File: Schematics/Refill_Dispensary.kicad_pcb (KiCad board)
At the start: 2 copper layers, 7.5 x 2 mm, 60 parts, among them J1 USB_B_Micro, J10 Switch 2, J11 Switch 3, J12 Switch 1, J2 Pot 1, J3 Barrel_Jack_Switch, J4 USB_BOOT, J5 Load Cell Power, J6 Load Cell Data, J7 Inductor 1, J8 Inductor 2, J9 Pot 2, Q1 TIP120, Q2 TIP120, SW4 SW_SPDT, U1 RP2040, U2 NCP1117-3.3_SOT223, U3 Flash Memory, U4 NHD-C0220BIZ, U5 AD622, Y1 Crystal

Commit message: organizing
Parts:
- moved J7 225.0 mm to (255.0, 144.9), turned to -90 degrees
- moved J8 207.7 mm to (255.8, 122.4), turned to -90 degrees
- moved R3 112.9 mm to (19.9, 59.1)
- moved R2 108.4 mm to (30.4, 58.5)
- moved J6 108.3 mm to (14.7, 164.6), turned to 90 degrees
- moved R1 105.1 mm to (40.6, 58.5), turned to 180 degrees
- moved J11 103.2 mm to (112.3, 68.6), turned to 180 degrees
- moved Q1 96.5 mm to (243.5, 136.1)
- moved J1 90.1 mm to (170.9, 33.8)
- moved J10 88.3 mm to (100.3, 68.8), turned to 180 degrees
- moved D3 86.9 mm to (17.4, 59.2), turned to 180 degrees
- moved C2 84.6 mm to (151.1, 50.2), turned to -90 degrees
- moved U2 84.1 mm to (158.6, 49.0), turned to -90 degrees
- moved C3 82.9 mm to (167.0, 51.4), turned to 90 degrees
- moved D2 81.0 mm to (27.6, 58.8), turned to 180 degrees
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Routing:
- net GND: vias 0 -> 2
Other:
- outline, holes or cut-outs redrawn
- board text added: "Load Cell"
- board text added: "Machine Status LEDs"
- board text added: "Notes: R1 is unconnected"
- board text added: "Power Supply"
- board text added: "UI Go Buttons"
- board text added: "User Interface"
- board text added: "Valve Control"

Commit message: everything is pretty
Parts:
- moved 1u1 142.0 mm to (55.6, 53.2), turned to 90 degrees
- moved C9 114.3 mm to (193.0, 79.9)
- moved C13 108.8 mm to (193.3, 84.8)
- moved C10 97.2 mm to (193.8, 95.1)
- moved C7 92.2 mm to (95.5, 87.9), turned to 180 degrees
- moved 10k2 91.9 mm to (104.8, 80.1), turned to 180 degrees
- moved C11 87.0 mm to (193.4, 89.6)
- moved C1 85.5 mm to (95.6, 92.3), turned to 180 degrees
- moved C12 83.6 mm to (102.7, 97.5)
- moved C6 73.6 mm to (79.3, 151.1), turned to 90 degrees
- moved R15 72.8 mm to (111.0, 101.2)
- moved R9 72.8 mm to (115.4, 101.2)
- moved R7 72.4 mm to (137.3, 153.3)
- moved C8 71.5 mm to (97.2, 97.7)
- moved C5 64.2 mm to (96.9, 151.1), turned to 90 degrees
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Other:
- outline, holes or cut-outs redrawn
- board text added: "Flash Mem"

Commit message: I'm cant make a PCB
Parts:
- added R13: 10k, Resistor_SMD:R_0201_0603Metric, F.Cu at (85.7, 65.3)
- R10: value R -> 10k
- moved J6 165.8 mm to (202.1, 105.4), turned to -90 degrees
- moved R12 135.6 mm to (178.4, 113.3), turned to 0 degrees
- moved U5 117.6 mm to (170.8, 106.0), turned to 90 degrees
- moved D6 117.0 mm to (164.5, 112.1), turned to 90 degrees
- moved D7 106.2 mm to (164.1, 101.4), turned to 90 degrees
- moved C13 100.3 mm to (95.5, 106.9)
- moved C11 95.1 mm to (102.2, 116.6), turned to 90 degrees
- moved J4 94.6 mm to (64.8, 85.1)
- moved R7 90.3 mm to (69.3, 93.9)
- moved C9 87.8 mm to (108.8, 105.0), turned to 180 degrees
- moved J5 84.5 mm to (107.6, 79.0), turned to 0 degrees
- moved C10 84.2 mm to (111.0, 110.5), turned to 180 degrees
- moved J11 71.4 mm to (48.6, 101.0), turned to -90 degrees
- moved R10 69.1 mm to (95.3, 67.4)
- moved J12 68.5 mm to (49.0, 125.6), turned to -90 degrees
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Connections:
- net Net-(C1-Pad2) renamed +1V1
- net Net-(C5-Pad2) renamed /CLK_IN
- net Net-(R11-Pad2) renamed /CLK_OUT
- D4 pad 1: Net-(J7-Pad1) -> GND
- D4 pad 2: +12V -> Net-(D4-Pad2)
- D5 pad 1: Net-(D5-Pad1) -> GND
- D5 pad 2: +12V -> Net-(D5-Pad2)
- J7 pad 1: Net-(J7-Pad1) -> GND
- J7 pad 2: +12V -> Net-(D4-Pad2)
- J8 pad 1: Net-(D5-Pad1) -> GND
- J8 pad 2: +12V -> Net-(D5-Pad2)
- Q1 pad 2: Net-(J7-Pad1) -> +12V
- Q1 pad 3: GND -> Net-(D4-Pad2)
- Q2 pad 2: Net-(D5-Pad1) -> +12V
- Q2 pad 3: GND -> Net-(D5-Pad2)
- R1 pad 1: unconnected-(R1-Pad1) -> GND
- U1 pad 4: unconnected-(U1-Pad4) -> /S_SDA
- U1 pad 5: unconnected-(U1-Pad5) -> /S_SCL
- U1 pad 6: /S_SDA -> unconnected-(U1-Pad6)
- U1 pad 7: /S_SCL -> unconnected-(U1-Pad7)
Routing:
- net +3.3V: track 0.00 -> 31.7 mm
- net Net-(C2-Pad1): track 0.00 -> 13.6 mm
- net +12V: track 0.00 -> 11.7 mm
- net Net-(J1-Pad1): track 0.00 -> 10.2 mm
- net +1V1: track 0.00 -> 9.89 mm
- net Net-(R15-Pad2): track 0.00 -> 5.68 mm
- net GND: track 0.00 -> 4.93 mm, vias 2 -> 1
- net Net-(R9-Pad2): track 0.00 -> 4.24 mm
- removed copper zone on B.Cu, net GND
- removed copper zone on F.Cu, net GND
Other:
- board text removed: "Flash Mem"
- board text removed: "Load Cell"
- board text removed: "Valve Control"

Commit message: I'm cant make a PCB again
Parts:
- removed 10k2: R, Resistor_SMD:R_0201_0603Metric
- removed 1u1: C, Capacitor_SMD:C_0201_0603Metric
- added ?: , , F.Cu at (102.4, 110.7)
- added ?: , , F.Cu at (101.0, 109.3)
- added ?: , , F.Cu at (103.6, 110.7)
- added ?: , , F.Cu at (101.0, 108.2)
- added ?: , , F.Cu at (102.4, 108.2)
- added ?: , , F.Cu at (101.0, 110.7)
- added ?: , , F.Cu at (103.6, 109.3)
- added ?: , , F.Cu at (103.6, 108.2)
- added ?: , , F.Cu at (102.4, 109.3)
- added C14: 1u, Capacitor_SMD:C_0201_0603Metric, F.Cu at (97.8, 168.3)
- moved J7 148.5 mm to (57.5, 97.2), turned to 90 degrees
- moved J8 143.6 mm to (57.3, 109.0), turned to 90 degrees
- moved H1 127.1 mm to (179.3, 56.5)
- moved H2 127.1 mm to (173.6, 50.8)
- moved H3 127.1 mm to (173.6, 56.5)
- moved H4 127.1 mm to (179.3, 50.8)
- moved U4 124.4 mm to (103.8, 149.2)
- moved D5 123.2 mm to (67.6, 95.8), turned to 90 degrees
- moved D4 122.6 mm to (72.7, 95.1), turned to 90 degrees
- moved Q1 105.6 mm to (73.7, 101.7), turned to 180 degrees
- moved Q2 100.3 mm to (73.4, 109.2), turned to 180 degrees
- moved D3 99.5 mm to (55.3, 152.2), turned to -90 degrees
- moved R3 96.8 mm to (59.7, 151.9), turned to 180 degrees
- moved D2 90.2 mm to (55.3, 145.8), turned to -90 degrees
- moved R2 87.0 mm to (59.7, 145.9), turned to 180 degrees
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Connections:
- D4 pad 1: GND -> Net-(D4-Pad1)
- D4 pad 2: Net-(D4-Pad2) -> +12V
- D5 pad 1: GND -> Net-(D5-Pad1)
- D5 pad 2: Net-(D5-Pad2) -> +12V
- J7 pad 1: GND -> Net-(D4-Pad1)
- J7 pad 2: Net-(D4-Pad2) -> +12V
- J8 pad 1: GND -> Net-(D5-Pad1)
- J8 pad 2: Net-(D5-Pad2) -> +12V
- Q1 pad 2: +12V -> Net-(D4-Pad1)
- Q1 pad 3: Net-(D4-Pad2) -> GND
- Q2 pad 2: +12V -> Net-(D5-Pad1)
- Q2 pad 3: Net-(D5-Pad2) -> GND
- U1 pad 11: /LED3 -> unconnected-(U1-Pad11)
- U1 pad 15: unconnected-(U1-Pad15) -> /LED1
- U1 pad 16: unconnected-(U1-Pad16) -> /LED2
- U1 pad 17: unconnected-(U1-Pad17) -> /LED3
- U1 pad 8: /LED1 -> unconnected-(U1-Pad8)
- U1 pad 9: /LED2 -> unconnected-(U1-Pad9)
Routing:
- net +12V: track 11.7 -> 95.5 mm
- net /S_SCL: track 0.00 -> 67.1 mm, vias 0 -> 1
- net /S_SDA: track 0.00 -> 66.8 mm, vias 0 -> 1
- net /LED3: track 0.00 -> 64.2 mm
- net /LED2: track 0.00 -> 60.8 mm
- net /USB_D+: track 0.00 -> 60.3 mm, vias 0 -> 2
- net /LED1: track 0.00 -> 56.4 mm
- net /SW3: track 0.00 -> 53.8 mm
- net /SW2: track 0.00 -> 47.6 mm
- net /P2: track 0.00 -> 46.2 mm, vias 0 -> 2
- net /P1: track 0.00 -> 45.3 mm, vias 0 -> 2
- net /SW1: track 0.00 -> 44.0 mm
- net /QSPI_SS: track 0.00 -> 37.7 mm
- net /USB_D-: track 0.00 -> 34.9 mm, vias 0 -> 2
- net /ADC0: track 0.00 -> 33.4 mm
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- added copper zone on F.Cu, net +12V
- added copper zone on F.Cu, net +3.3V
- added copper zone on B.Cu, net GND
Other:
- board size 7.5 x 2 mm -> 205.6 x 165.7 mm
- board text removed: "Machine Status LEDs"
- board text removed: "Notes: R1 is unconnected"
- board text removed: "Power Supply"
- board text removed: "UI Go Buttons"
- board text removed: "User Interface"

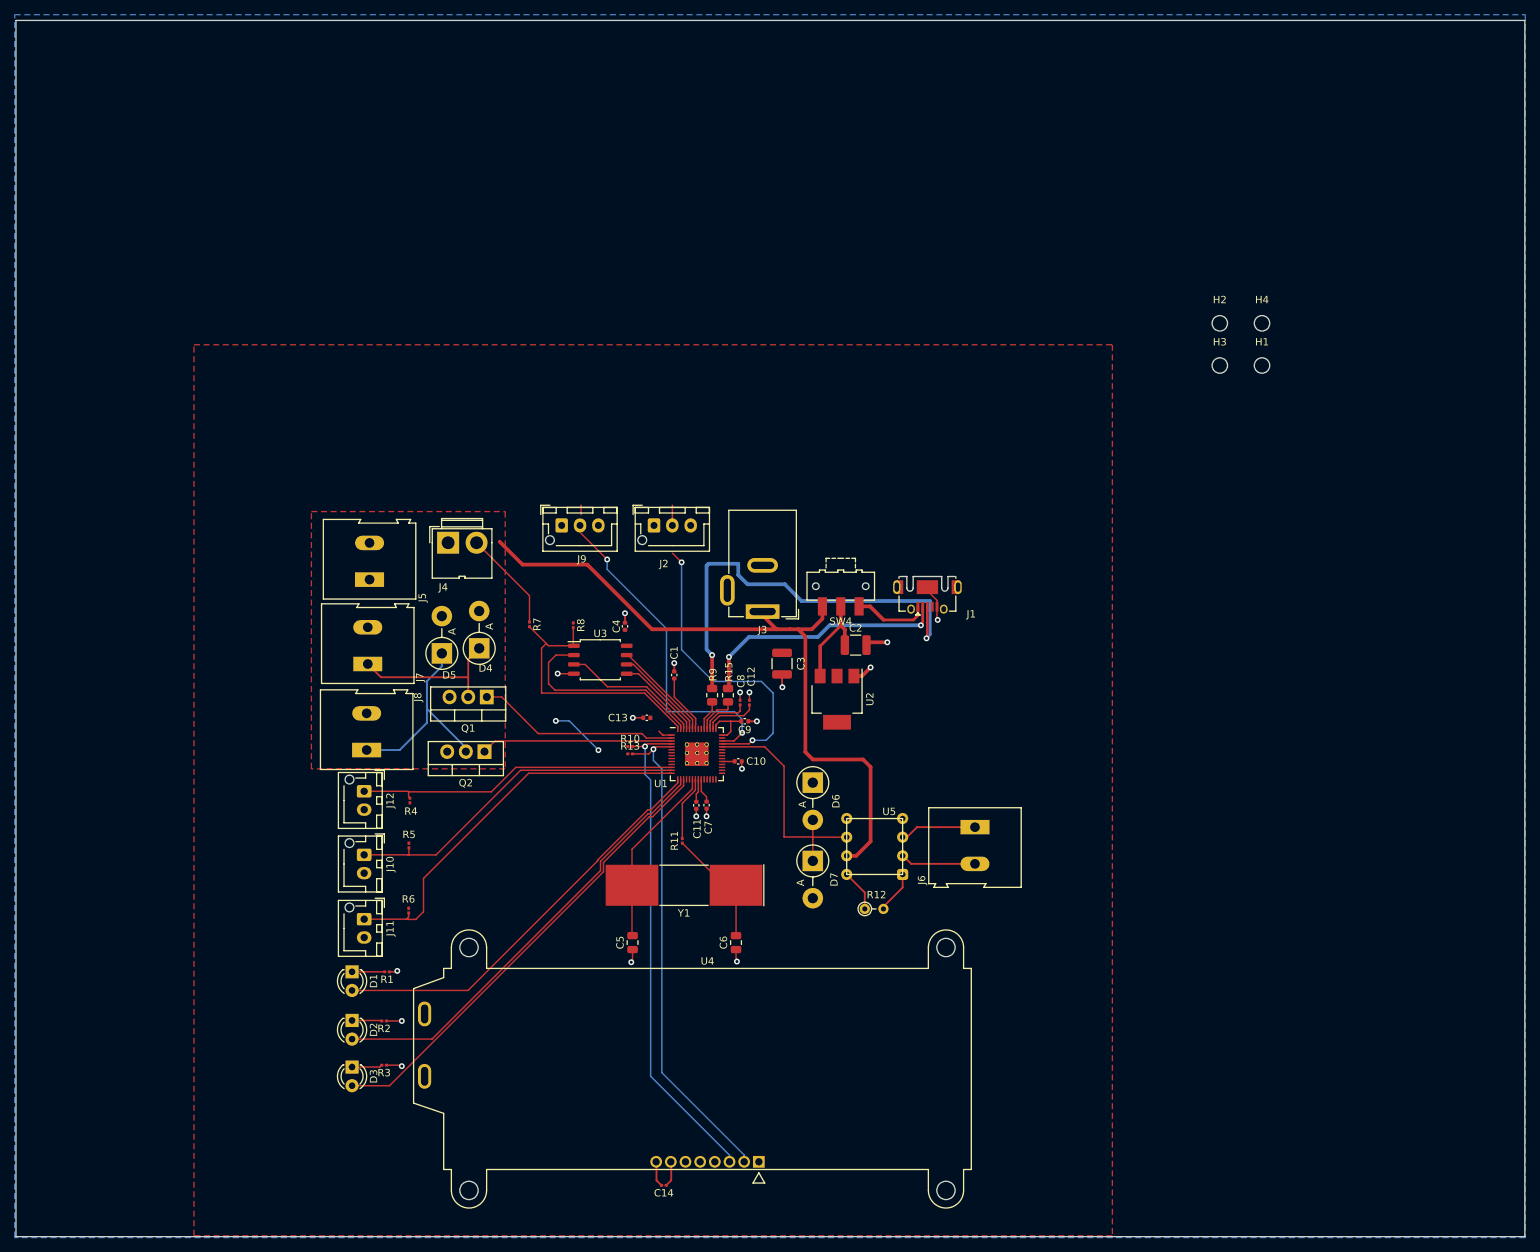
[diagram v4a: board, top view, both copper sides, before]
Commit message: board mostly finished
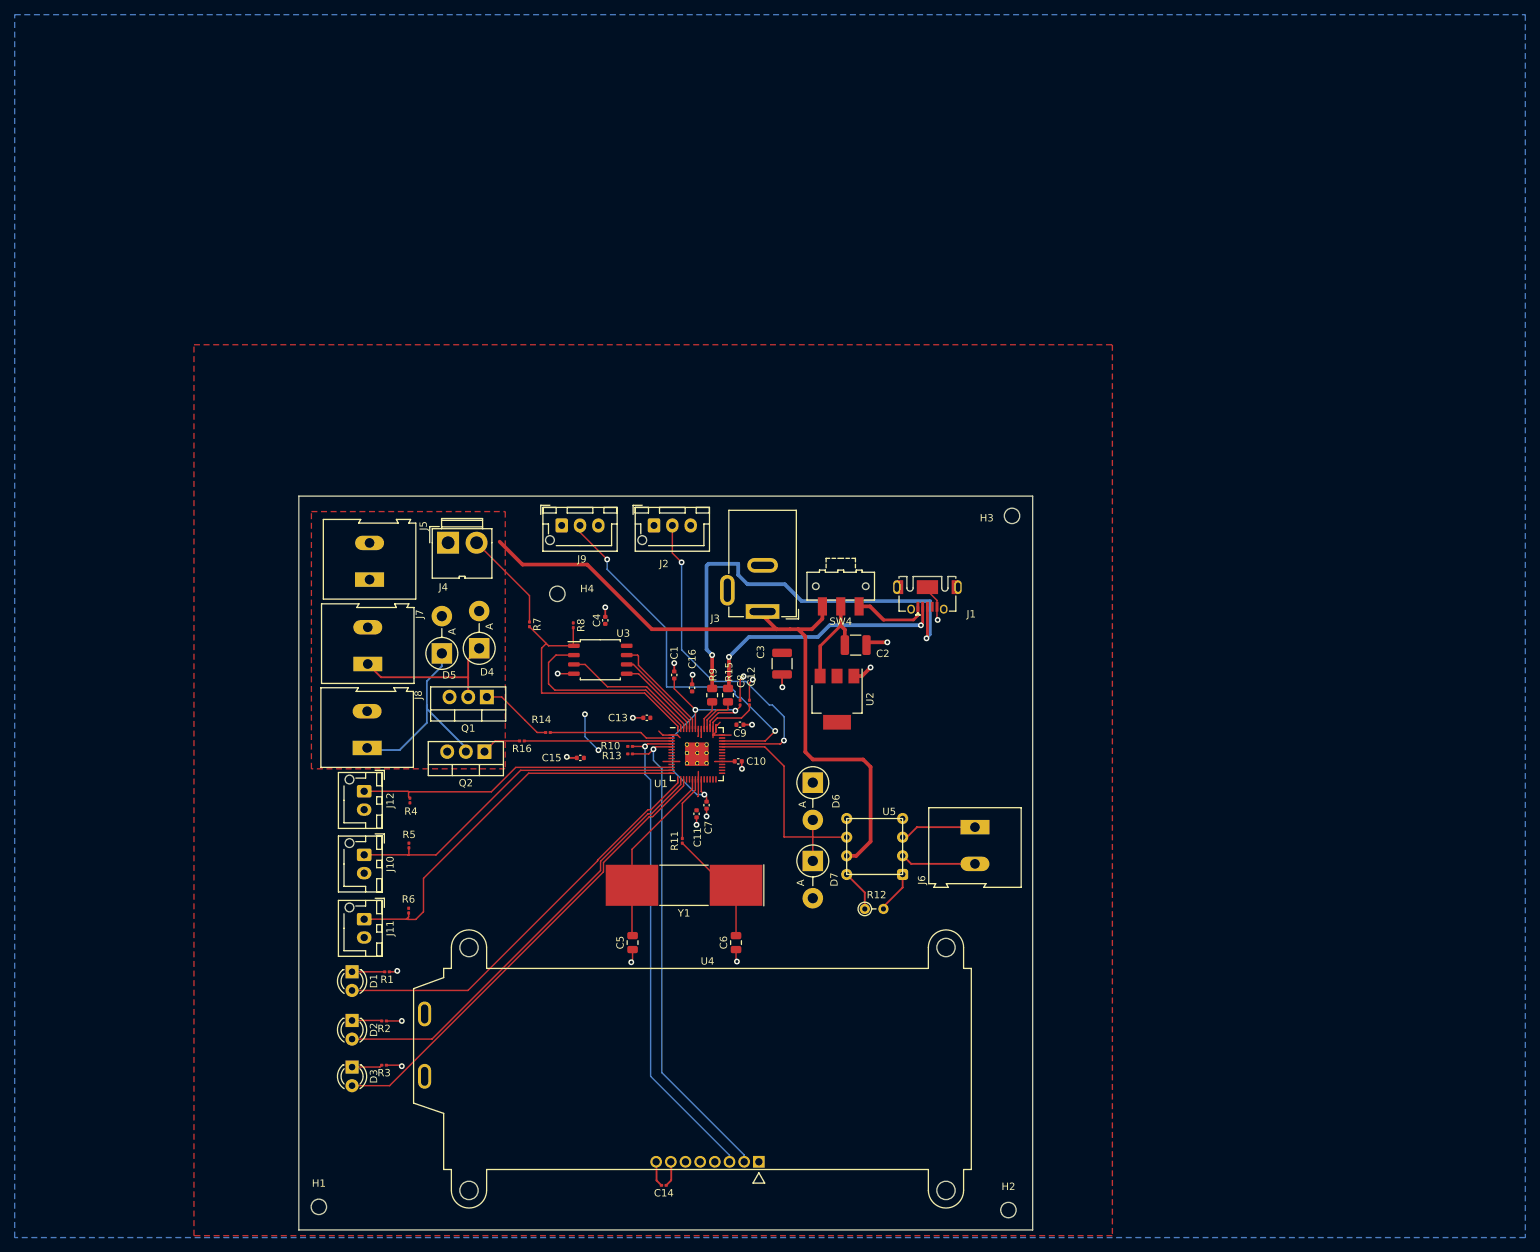
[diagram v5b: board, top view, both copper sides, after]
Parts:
- added C15: 100n, Capacitor_SMD:C_0402_1005Metric, F.Cu at (86.4, 110.0)
- added C16: 100n, Capacitor_SMD:C_0402_1005Metric, F.Cu at (101.7, 100.5)
- added R14: 10k, Resistor_SMD:R_0201_0603Metric, F.Cu at (82.0, 106.6)
- added R16: 10k, Resistor_SMD:R_0201_0603Metric, F.Cu at (78.5, 107.7)
- moved H1 172.2 mm to (50.8, 171.2)
- moved H2 124.2 mm to (144.8, 171.6)
- moved H4 102.9 mm to (83.3, 87.7)
- moved H3 35.0 mm to (145.3, 77.0)
- moved C4 2.81 mm to (89.8, 91.3)
- moved C11 1.15 mm to (102.3, 117.6)
- moved C9 0.81 mm to (108.2, 105.5)
- moved J8 0.30 mm to (57.4, 108.7)
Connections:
- Q1 pad 1: /V1 -> Net-(Q1-Pad1)
- Q2 pad 1: /V2 -> Net-(Q2-Pad1)
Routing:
- net +1V1: track 17.9 -> 38.3 mm, vias 0 -> 3
- net /V1: track 27.5 -> 16.8 mm
- net Net-(Q1-Pad1): track 0.00 -> 10.0 mm
- net GND: track 33.8 -> 40.9 mm, vias 19 -> 21
- net /V2: track 26.1 -> 19.9 mm
- net /P2: track 46.2 -> 52.2 mm
- net Net-(Q2-Pad1): track 0.00 -> 5.24 mm
- net +3.3V: track 28.8 -> 32.7 mm
- net /P1: track 45.3 -> 47.1 mm
- net /QSPI_SD3: track 13.9 -> 14.6 mm
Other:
- board size 205.6 x 165.7 mm -> 100 x 100 mm

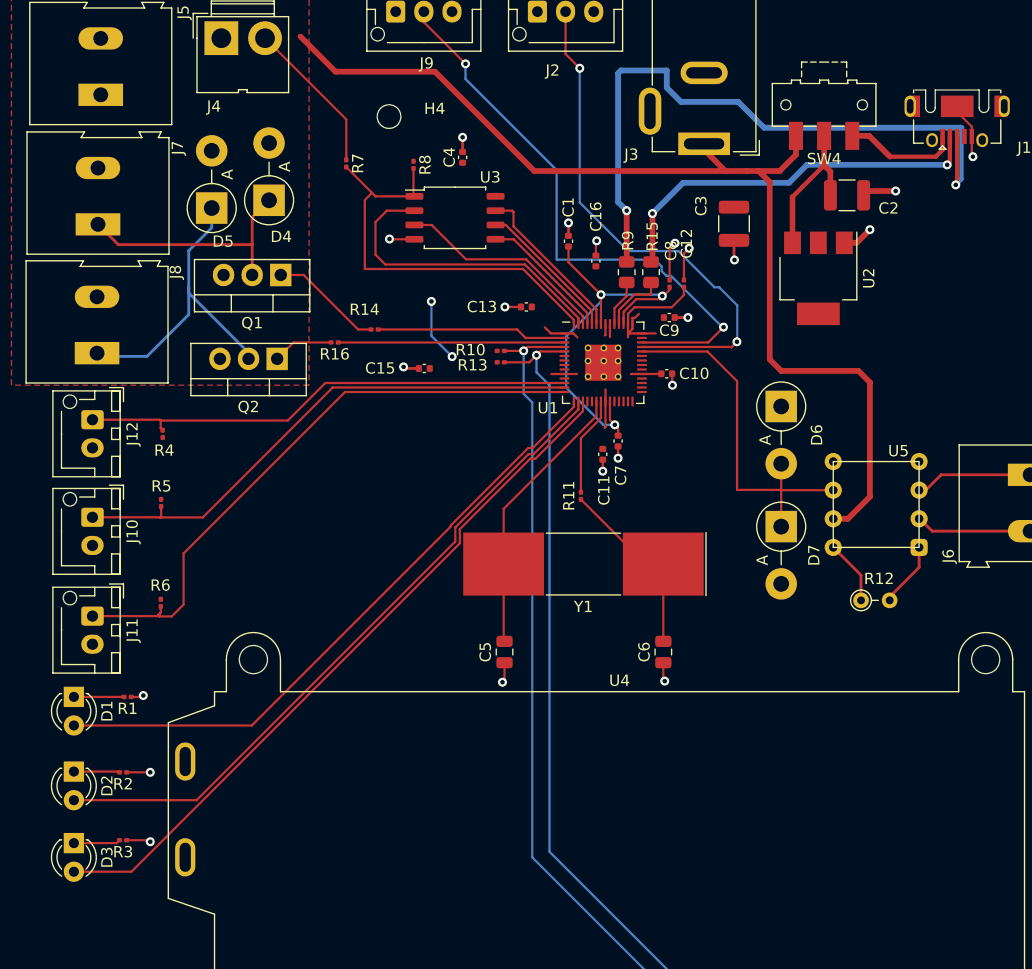
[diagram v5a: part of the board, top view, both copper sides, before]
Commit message: update screen schematic
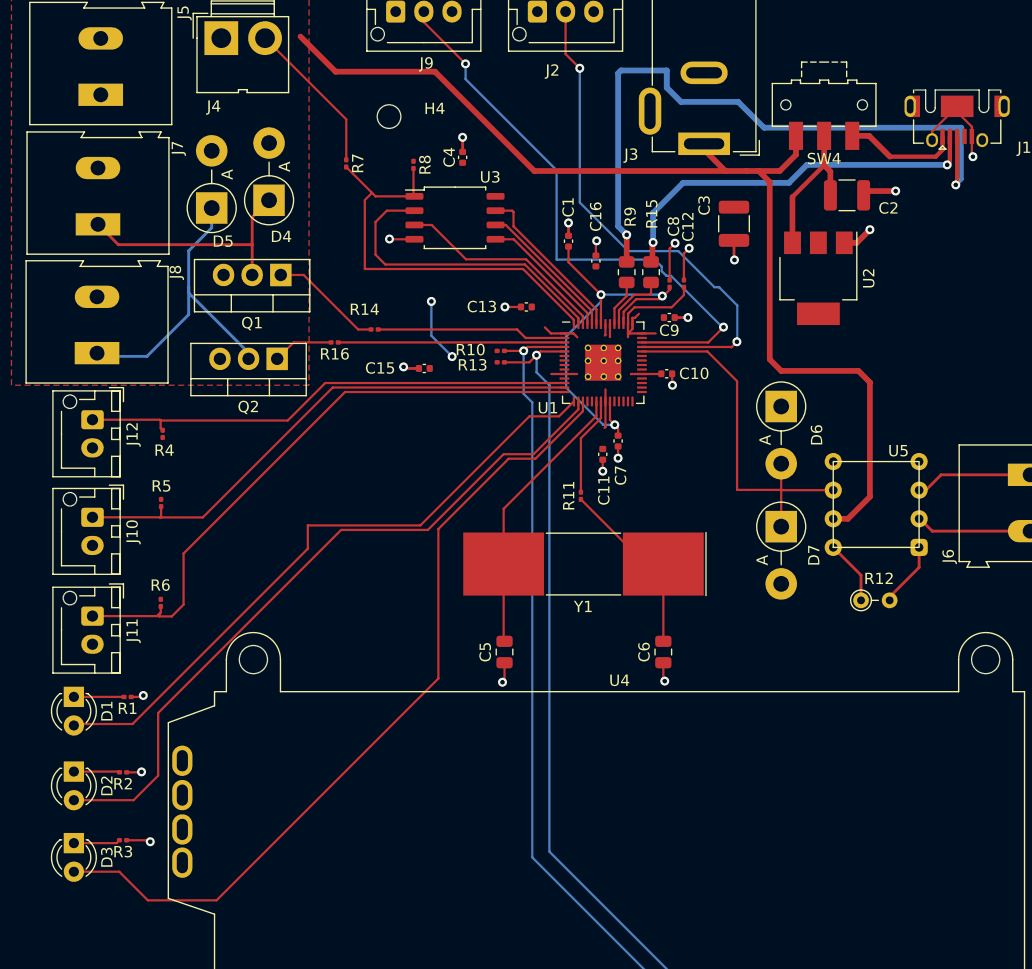
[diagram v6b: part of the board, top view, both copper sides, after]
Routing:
- net /LED3: track 64.2 -> 73.3 mm
- net GND: track 40.9 -> 44.1 mm
- net /LED2: track 60.8 -> 63.3 mm
- net /LED1: track 56.4 -> 57.3 mm

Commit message: board v1
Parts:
- added 12V: TestPoint_Pad_D1.0mm, TestPoint:TestPoint_Pad_D1.0mm, F.Cu at (100.6, 90.6)
- added ADC: TestPoint_Pad_D1.0mm, TestPoint:TestPoint_Pad_D1.0mm, F.Cu at (112.1, 116.7)
- added GND: TestPoint_Pad_D4.0mm, TestPoint:TestPoint_Pad_D4.0mm, F.Cu at (138.3, 94.9)
- added GND: TestPoint_Pad_D2.0mm, TestPoint:TestPoint_Pad_D2.0mm, F.Cu at (96.9, 87.2)
- added J13: SWD, Connector_JST:JST_XH_B3B-XH-AM_1x03_P2.50mm_Vertical, F.Cu at (143.7, 164.6)
- added J14: SWD, Connector_JST:JST_XH_B3B-XH-AM_1x03_P2.50mm_Vertical, F.Cu at (143.3, 113.3)
- moved D6 0.97 mm to (119.1, 113.4)
- moved D7 0.97 mm to (119.1, 124.1)
- moved R12 0.97 mm to (126.2, 130.6)
- moved U5 0.97 mm to (118.6, 123.4)
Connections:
- U1 pad 24: unconnected-(U1-Pad24) -> /SWCLK
- U1 pad 25: unconnected-(U1-Pad25) -> /SWD
- U5 pad 5: GND -> Net-(U5-Pad5)
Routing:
- net /SWCLK: track 0.00 -> 65.9 mm
- net /SWD: track 0.00 -> 64.3 mm
- net Net-(U5-Pad5): track 0.00 -> 23.7 mm
- net GND: track 44.1 -> 64.9 mm
- net +3.3V: track 32.7 -> 51.4 mm, vias 2 -> 4
- net /ADC0: track 33.3 -> 36.4 mm
- net +12V: track 95.5 -> 98.4 mm
- net /Load_cell+: track 10.2 -> 9.26 mm
- net /LED1: track 57.3 -> 56.4 mm
- net /S_SCL: track 67.1 -> 67.7 mm
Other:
- board text added: "REFILL DISPENSERY V1 TEAM 18"
